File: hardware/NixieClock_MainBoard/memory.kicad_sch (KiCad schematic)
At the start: 3 parts, among them J7 Micro_SD_Card

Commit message: display 1.14 anpassungen. Stecker war verpolt
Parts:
- J7: footprint Connector_Card:microSD_HC_Molex_47219-2001 -> Connector_Card:microSD_HC_Hirose_DM3D-SF
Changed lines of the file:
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@@
 			)
 		)
-		(property "Footprint" "Connector_Card:microSD_HC_Molex_47219-2001"
+		(property "Footprint" "Connector_Card:microSD_HC_Hirose_DM3D-SF"
 			(at 41.91 68.58 0)
 			(effects

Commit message: V2.0 release fertig.
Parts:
- added C23: 100nF, Capacitor_SMD:C_0603_1608Metric, symbol Device:C
- added U20, U21: NC7SZ125M5X, Package_TO_SOT_SMD:SOT-23-5, symbol 74xGxx:NC7SZ125M5X
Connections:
- net +3.3V: now also C23.1, U20.5 (VCC), U21.5 (VCC)
- net CS_MEM_1: now also U20.1 (~{OE}), U21.1 (~{OE})
- net GND: now also C23.2, U20.3 (GND), U21.3 (GND)
- net MISO: now also U21.4 (Y); no longer J7.7 (DAT0)
- net MOSI: now also U20.2 (A); no longer J7.3 (CMD)
- new net: J7.3 (CMD), U20.4 (Y)
- new net: J7.7 (DAT0), U21.2 (A)
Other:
- moved on the sheet: C5, C6

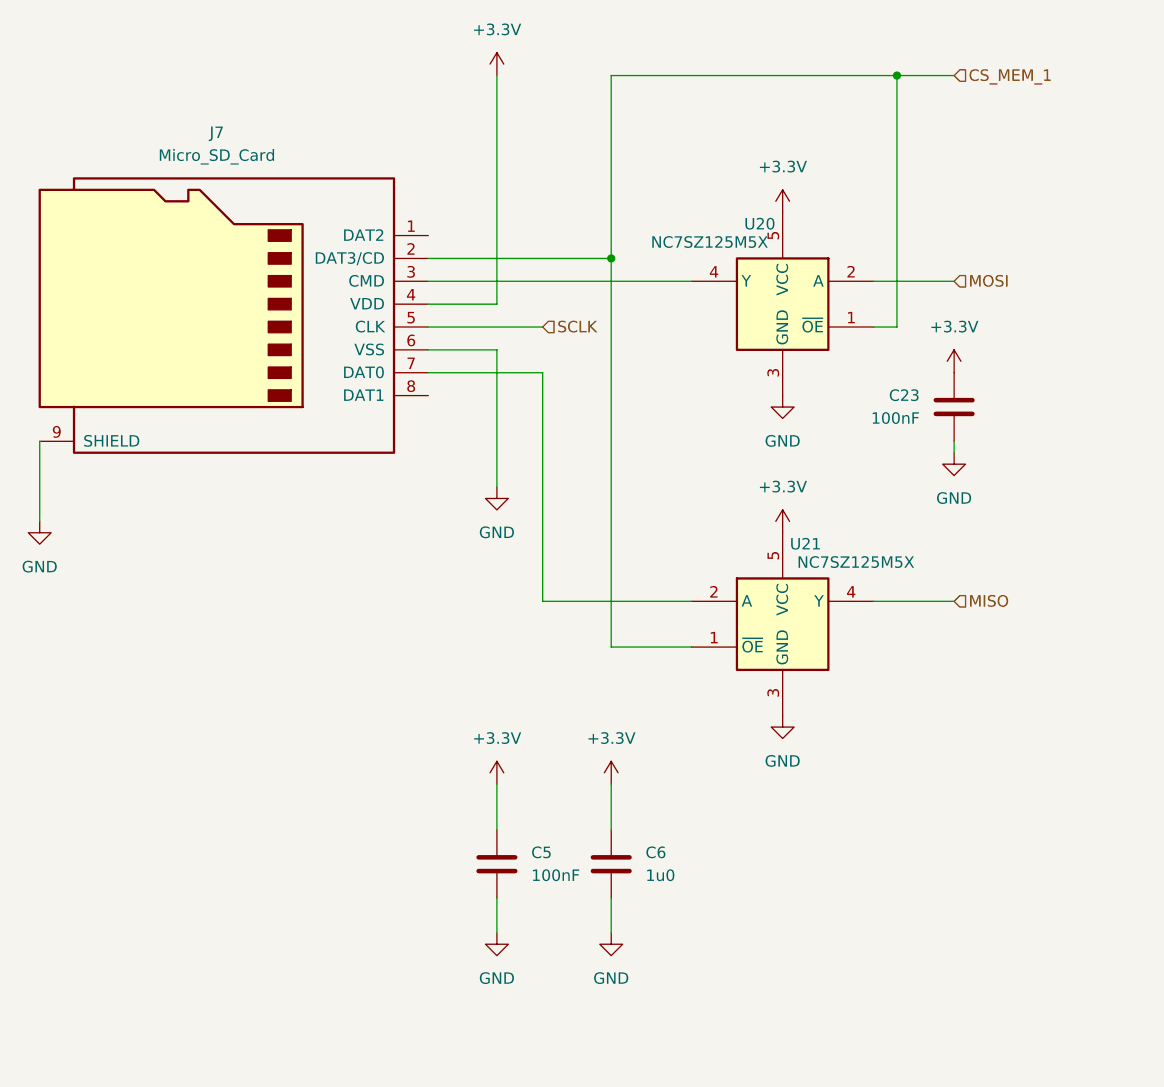
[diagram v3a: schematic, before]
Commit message: Hardware V2.1 add NixieClock_MainBoard/NixieClock_Schematic.pdf
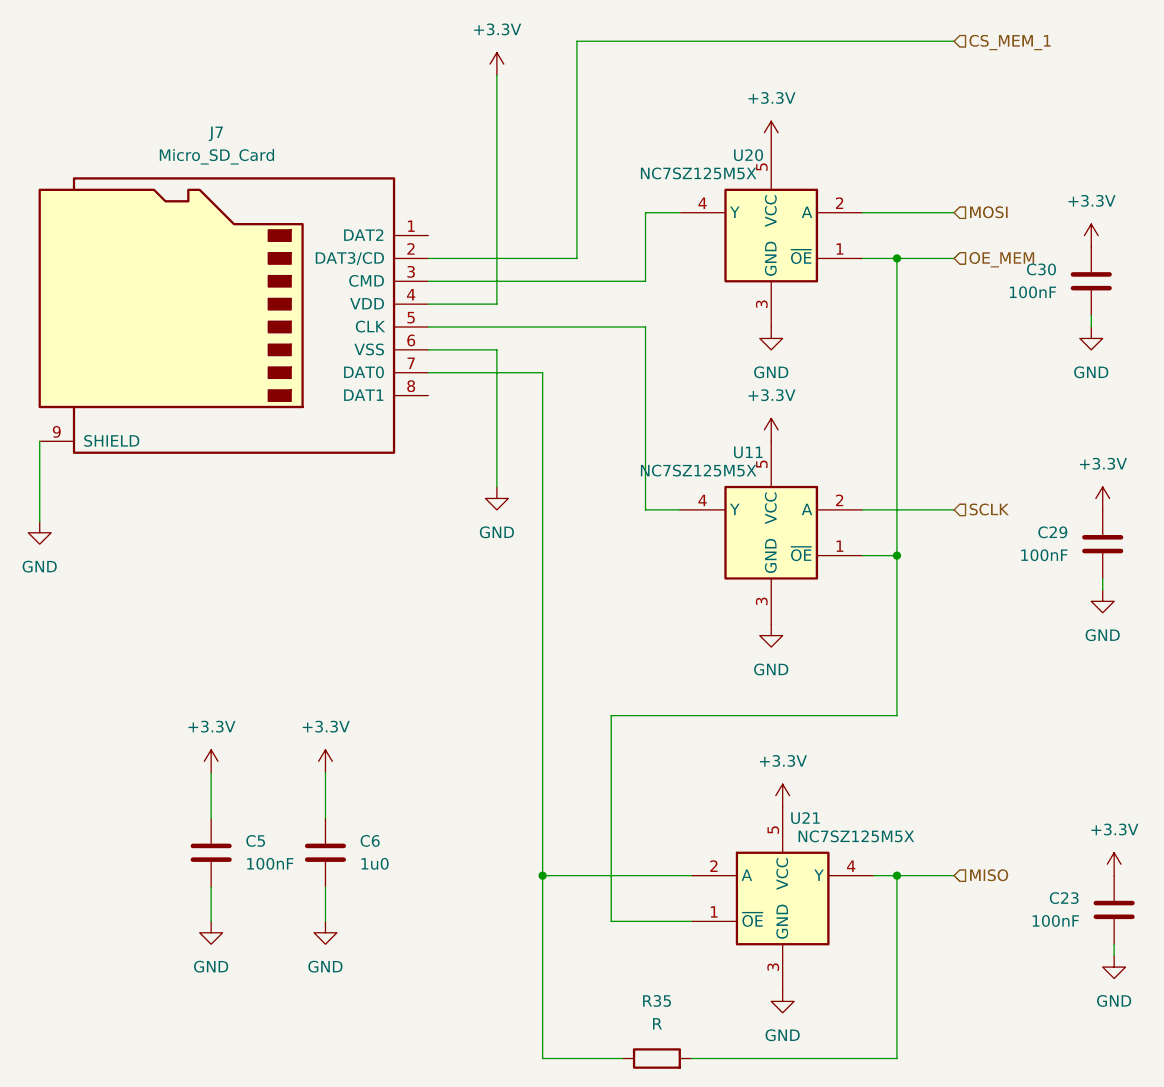
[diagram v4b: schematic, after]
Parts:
- added C29, C30: 100nF, Capacitor_SMD:C_0603_1608Metric, symbol Device:C
- added R35: R, Resistor_SMD:R_0603_1608Metric, symbol Device:R
- added U11: NC7SZ125M5X, Package_TO_SOT_SMD:SOT-23-5, symbol 74xGxx:NC7SZ125M5X
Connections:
- net +3.3V: now also C29.1, C30.1, U11.5 (VCC)
- net CS_MEM_1: no longer U20.1 (~{OE}), U21.1 (~{OE})
- net GND: now also C29.2, C30.2, U11.3 (GND)
- net MISO: now also R35.2
- net SCLK: now also U11.2 (A); no longer J7.5 (CLK)
- net at J7.7 (DAT0), U21.2 (A): now also R35.1
- new net: J7.5 (CLK), U11.4 (Y)
- new net OE_MEM: U11.1 (~{OE}), U20.1 (~{OE}), U21.1 (~{OE})
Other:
- moved on the sheet: C23, C5, C6, U20, U21
